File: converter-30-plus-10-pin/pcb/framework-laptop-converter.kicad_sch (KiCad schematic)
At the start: 6 parts, among them J1 20879-040E-01, J2 FFC2B28-40-G

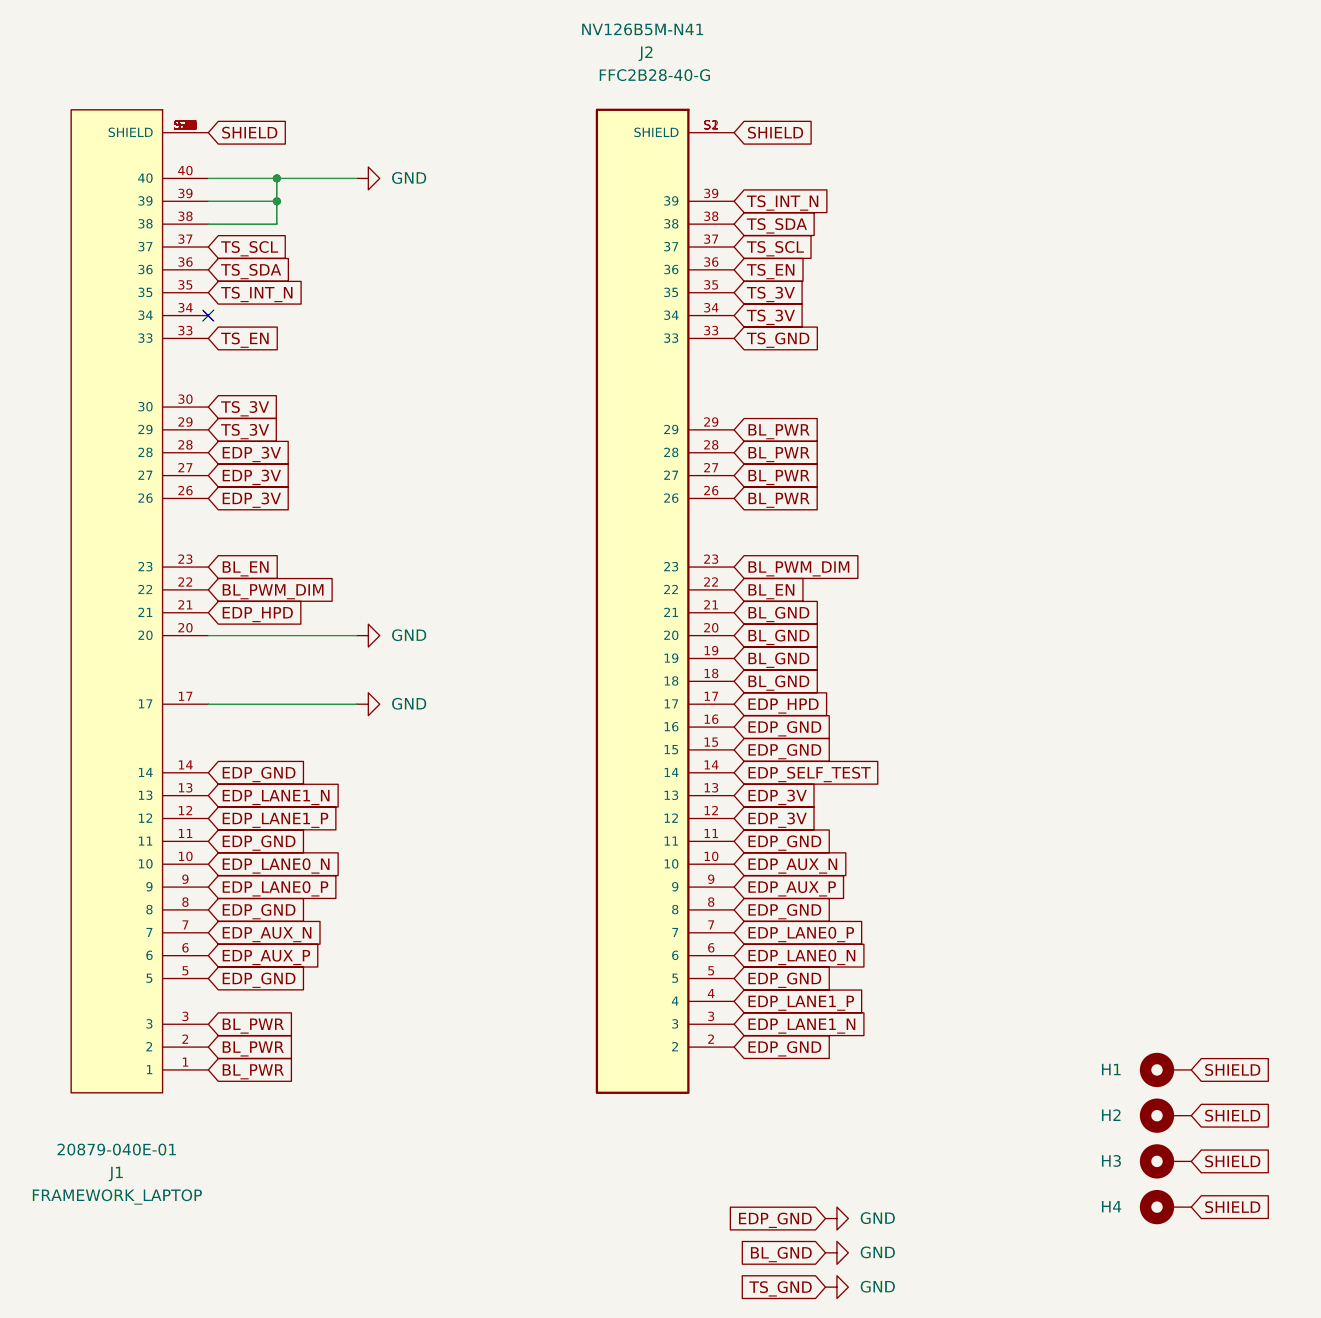
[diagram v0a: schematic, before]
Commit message: start migrating converter to framework's true pinout
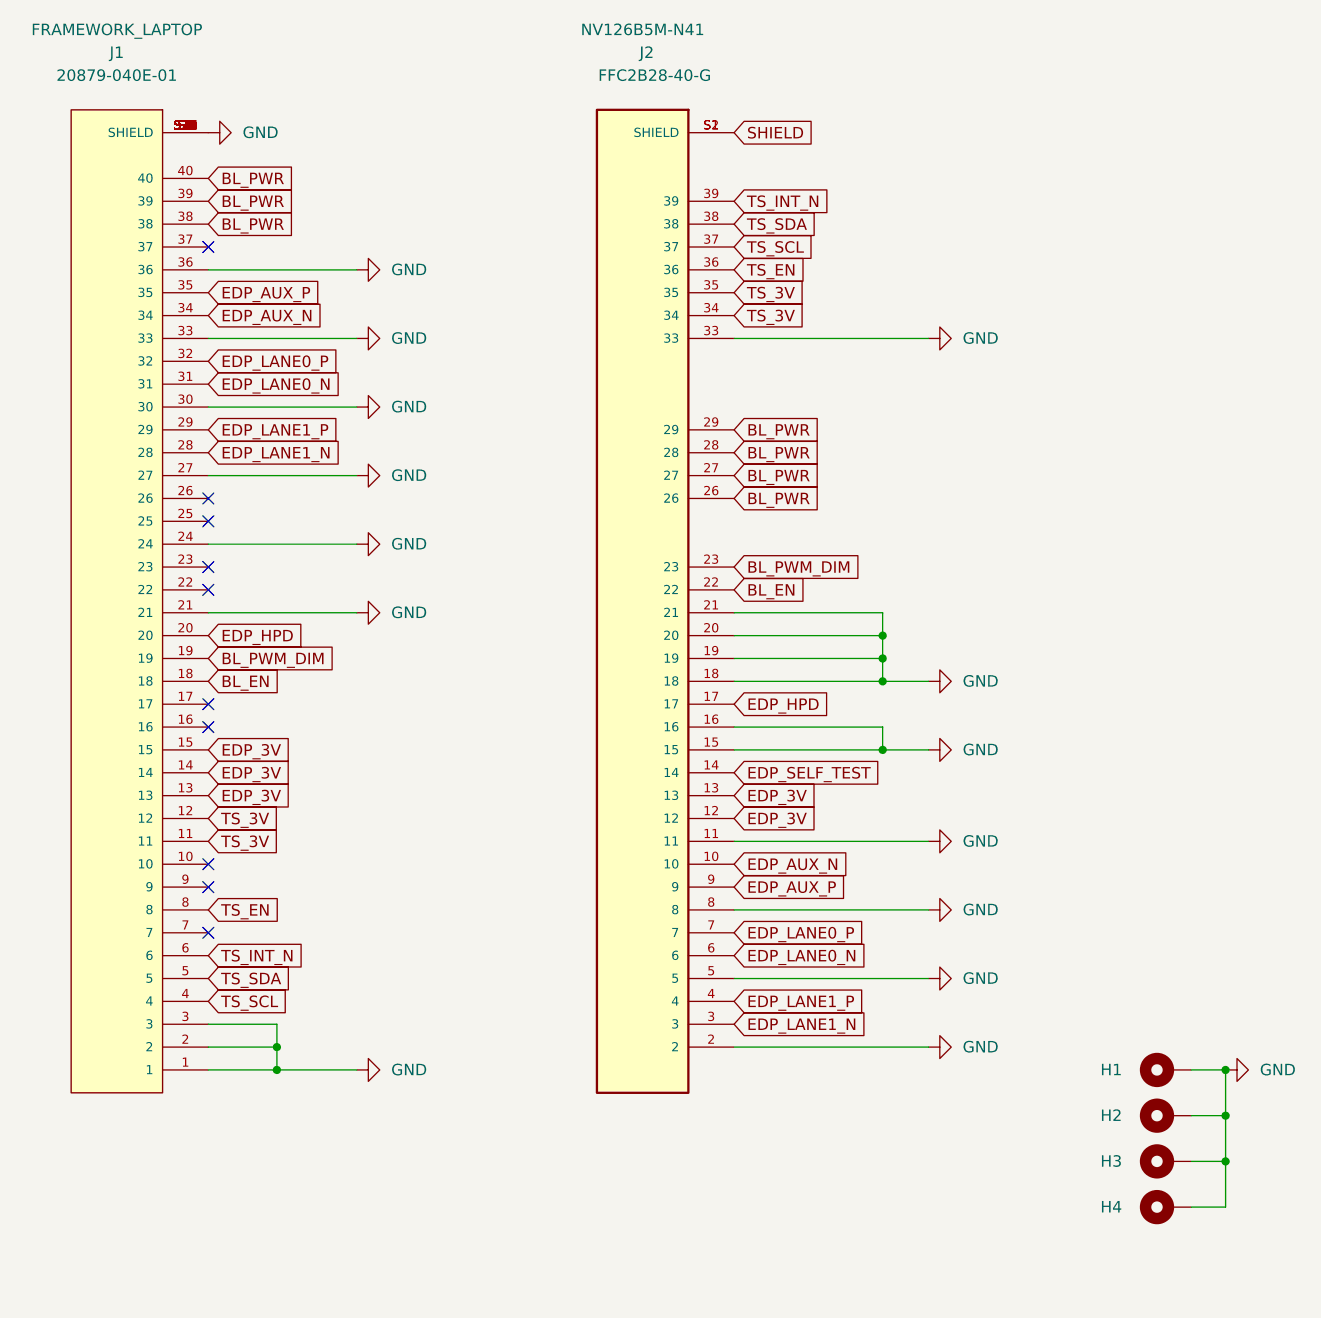
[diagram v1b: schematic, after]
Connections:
- net BL_EN: now also J1.18; no longer J1.23
- net BL_PWM_DIM: now also J1.19; no longer J1.22
- net BL_PWR: now also J1.38, J1.39, J1.40; no longer J1.1, J1.2, J1.3
- net EDP_3V: now also J1.13, J1.14, J1.15; no longer J1.26, J1.27, J1.28
- net EDP_AUX_N: now also J1.34; no longer J1.7
- net EDP_AUX_P: now also J1.35; no longer J1.6
- net EDP_HPD: now also J1.20; no longer J1.21
- net EDP_LANE0_N: now also J1.31; no longer J1.10
- net EDP_LANE0_P: now also J1.32; no longer J1.9
- net EDP_LANE1_N: now also J1.28; no longer J1.13
- net EDP_LANE1_P: now also J1.29; no longer J1.12
- net GND: now also H1.1, H2.1, H3.1, H4.1, J1.1, J1.2, J1.21, J1.24, J1.27, J1.3, J1.30, J1.33, J1.36, J1.S1 (SHIELD), J1.S10 (SHIELD), J1.S11 (SHIELD), J1.S12 (SHIELD), J1.S13 (SHIELD), J1.S14 (SHIELD), J1.S15 (SHIELD), J1.S16 (SHIELD), J1.S17 (SHIELD), J1.S18 (SHIELD), J1.S19 (SHIELD), J1.S2 (SHIELD), J1.S20 (SHIELD), J1.S21 (SHIELD), J1.S22 (SHIELD), J1.S23 (SHIELD), J1.S24 (SHIELD), J1.S25 (SHIELD), J1.S26 (SHIELD), J1.S27 (SHIELD), J1.S28 (SHIELD), J1.S29 (SHIELD), J1.S3 (SHIELD), J1.S30 (SHIELD), J1.S31 (SHIELD), J1.S32 (SHIELD), J1.S33 (SHIELD), J1.S34 (SHIELD), J1.S4 (SHIELD), J1.S5 (SHIELD), J1.S6 (SHIELD), J1.S7 (SHIELD), J1.S8 (SHIELD), J1.S9 (SHIELD); no longer J1.11, J1.14, J1.17, J1.20, J1.38, J1.39, J1.40, J1.5, J1.8
- net SHIELD: no longer H1.1, H2.1, H3.1, H4.1, J1.S1 (SHIELD), J1.S10 (SHIELD), J1.S11 (SHIELD), J1.S12 (SHIELD), J1.S13 (SHIELD), J1.S14 (SHIELD), J1.S15 (SHIELD), J1.S16 (SHIELD), J1.S17 (SHIELD), J1.S18 (SHIELD), J1.S19 (SHIELD), J1.S2 (SHIELD), J1.S20 (SHIELD), J1.S21 (SHIELD), J1.S22 (SHIELD), J1.S23 (SHIELD), J1.S24 (SHIELD), J1.S25 (SHIELD), J1.S26 (SHIELD), J1.S27 (SHIELD), J1.S28 (SHIELD), J1.S29 (SHIELD), J1.S3 (SHIELD), J1.S30 (SHIELD), J1.S31 (SHIELD), J1.S32 (SHIELD), J1.S33 (SHIELD), J1.S34 (SHIELD), J1.S4 (SHIELD), J1.S5 (SHIELD), J1.S6 (SHIELD), J1.S7 (SHIELD), J1.S8 (SHIELD), J1.S9 (SHIELD)
- net TS_3V: now also J1.11, J1.12; no longer J1.29, J1.30
- net TS_EN: now also J1.8; no longer J1.33
- net TS_INT_N: now also J1.6; no longer J1.35
- net TS_SCL: now also J1.4; no longer J1.37
- net TS_SDA: now also J1.5; no longer J1.36
- no-connect marks 1 -> 10

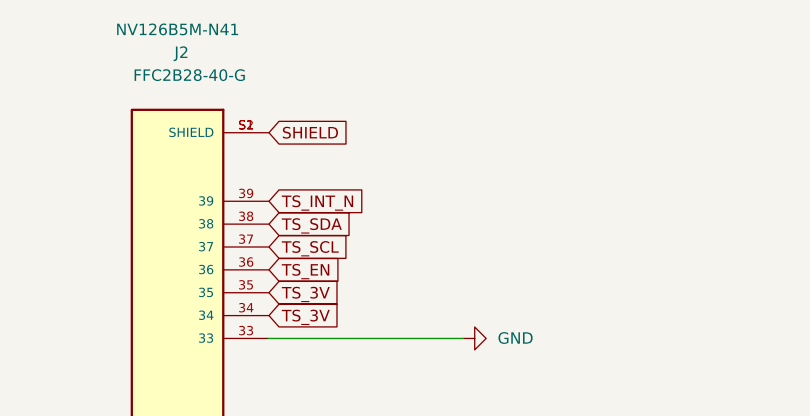
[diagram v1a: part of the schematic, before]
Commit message: converter: route edp lane 0 and aux + fix shield to ground
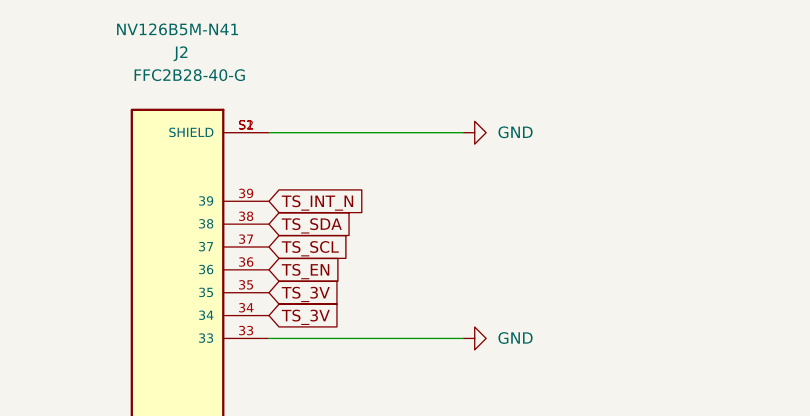
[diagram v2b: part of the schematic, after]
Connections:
- net SHIELD is gone; now on net GND: J2.S1 (SHIELD), J2.S2 (SHIELD)
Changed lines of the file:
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@@
+    (stroke (width 0) (type default) (color 0 0 0 0))
+  )
+  (wire (pts (xy 106.68 34.29) (xy 128.27 34.29))
     (stroke (width 0) (type default) (color 0 0 0 0))
   )
@@
     (effects (font (size 1.27 1.27)) (justify left))
     (property "Intersheet References" "${INTERSHEET_REFS}" (id 0) (at 57.6279 105.4894 0)
-      (effects (font (size 1.27 1.27)) (justify left) hide)
-    )
-  )
-  (global_label "SHIELD" (shape input) (at 106.68 34.29 0) (fields_autoplaced)
-    (effects (font (size 1.27 1.27)) (justify left))
-    (property "Intersheet References" "${INTERSHEET_REFS}" (id 0) (at 115.685 34.2106 0)
       (effects (font (size 1.27 1.27)) (justify left) hide)
     )
@@
     (pin "1")
   )
+  (symbol (lib_id "power:GND") (at 128.27 34.29 90) (unit 1)
+    (in_bom yes) (on_board yes) (fields_autoplaced)
+    (property "Reference" "#PWR?" (id 0) (at 134.62 34.29 0)
+      (effects (font (size 1.27 1.27)) hide)
+    )
+    (property "Value" "GND" (id 1) (at 132.08 34.2899 90)
+      (effects (font (size 1.27 1.27)) (justify right))
+    )
+    (property "Footprint" "" (id 2) (at 128.27 34.29 0)
+      (effects (font (size 1.27 1.27)) hide)
+    )
+    (property "Datasheet" "" (id 3) (at 128.27 34.29 0)
+      (effects (font (size 1.27 1.27)) hide)
+    )
+    (pin "1")
+  )
   (symbol (lib_id "Mechanical:MountingHole_Pad") (at 154.94 153.67 90) (unit 1)
     (in_bom yes) (on_board yes)
@@
       (reference "#PWR?") (unit 1) (value "GND") (footprint "")
     )
+    (path "/c65484eb-d2ac-483c-9646-1659e2d72b96"
+      (reference "#PWR?") (unit 1) (value "GND") (footprint "")
+    )

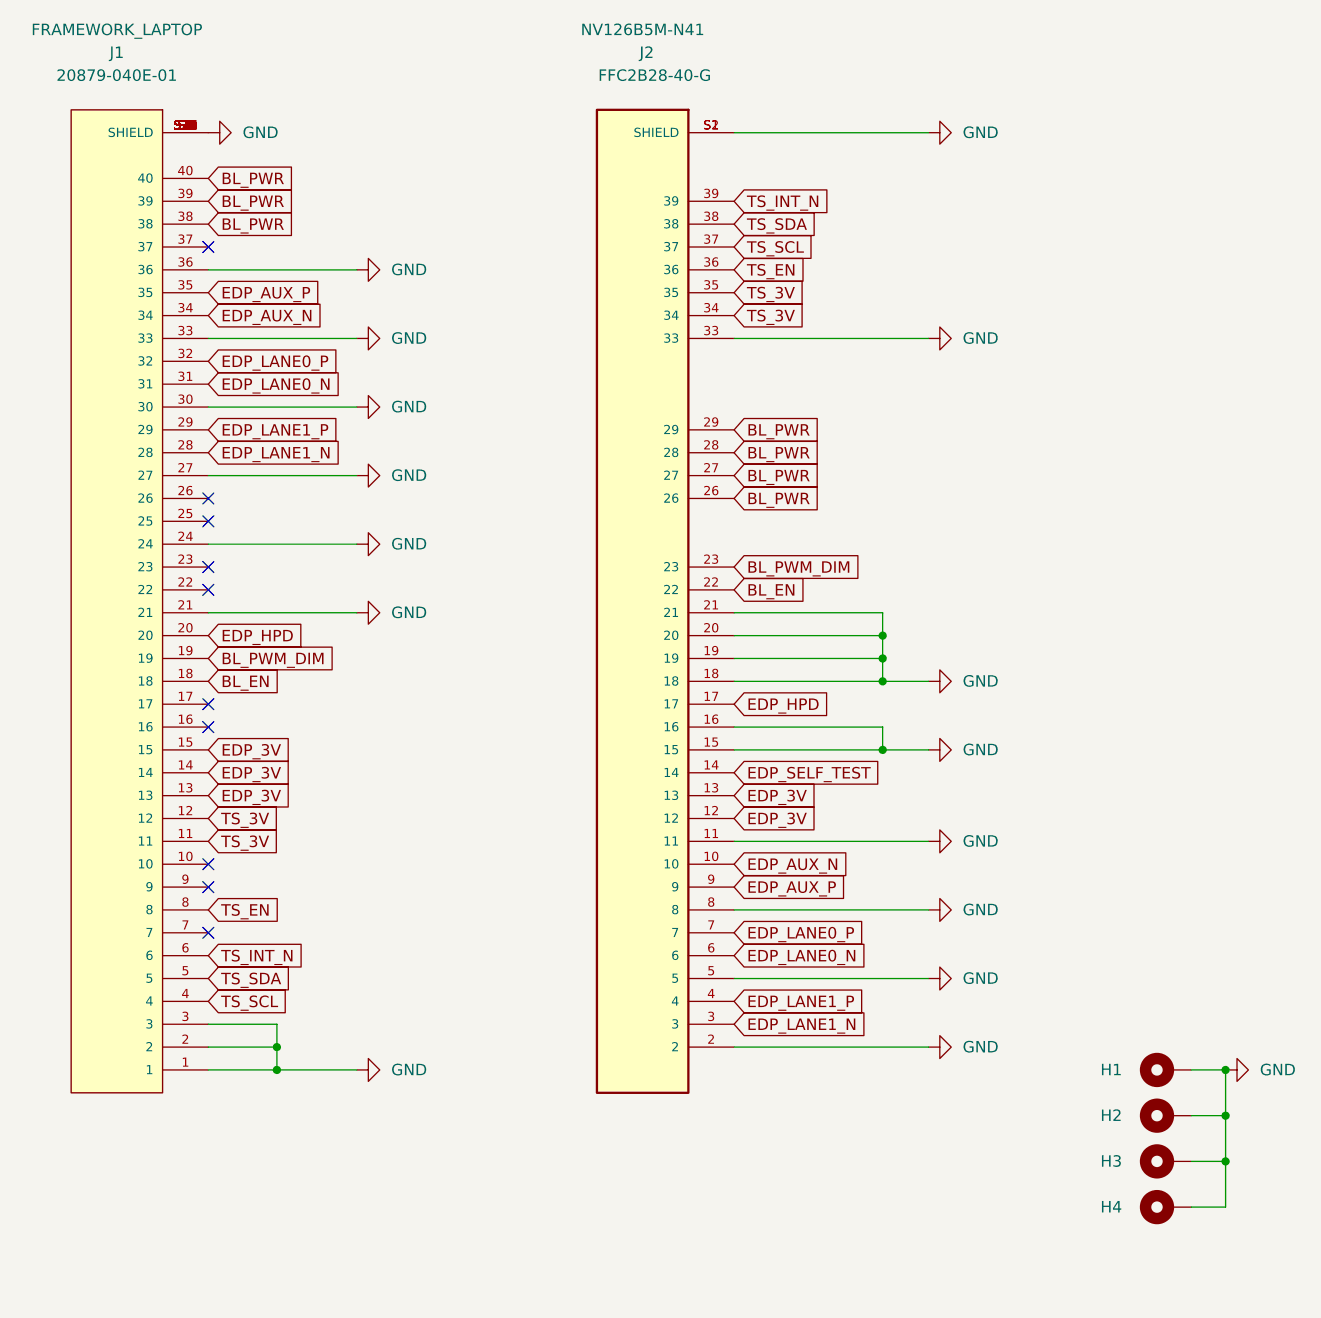
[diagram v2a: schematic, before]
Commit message: redo converter to use the 20455-040E
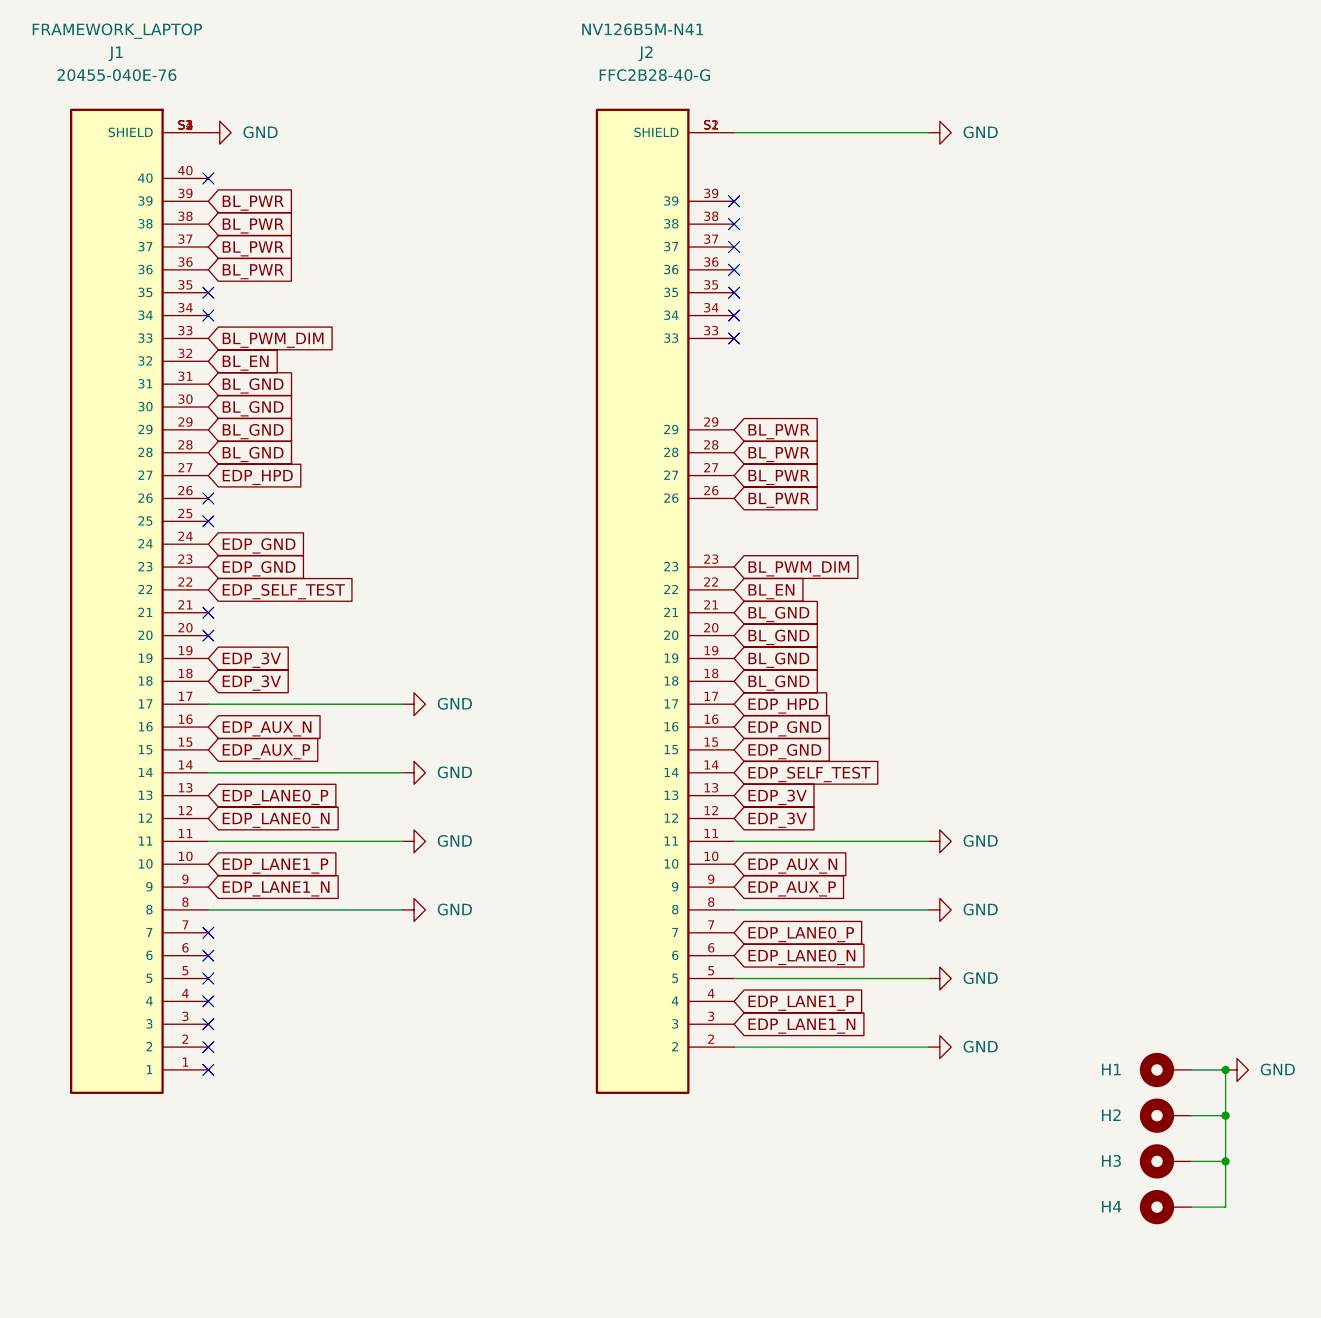
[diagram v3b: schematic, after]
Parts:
- J1: value 20879-040E-01 -> 20455-040E-76; footprint IPEX_20879-040E-01 -> IPEX_20455-040E-76; symbol 20879-040E-01:20879-040E-01 -> 20455-040E-76:20455-040E-76; STANDARD Manufacturer recommendations -> Manufacturer Recommendations
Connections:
- net BL_EN: now also J1.32; no longer J1.18
- net BL_PWM_DIM: now also J1.33; no longer J1.19
- net BL_PWR: now also J1.36, J1.37; no longer J1.40
- net EDP_3V: now also J1.18, J1.19; no longer J1.13, J1.14, J1.15
- net EDP_AUX_N: now also J1.16; no longer J1.34
- net EDP_AUX_P: now also J1.15; no longer J1.35
- net EDP_HPD: now also J1.27; no longer J1.20
- net EDP_LANE0_N: now also J1.12; no longer J1.31
- net EDP_LANE0_P: now also J1.13; no longer J1.32
- net EDP_LANE1_N: now also J1.9; no longer J1.28
- net EDP_LANE1_P: now also J1.10; no longer J1.29
- net EDP_SELF_TEST: now also J1.22
- net GND: now also J1.11, J1.14, J1.17, J1.8; no longer J1.1, J1.2, J1.21, J1.24, J1.27, J1.3, J1.30, J1.33, J1.36, J1.S10 (SHIELD), J1.S11 (SHIELD), J1.S12 (SHIELD), J1.S13 (SHIELD), J1.S14 (SHIELD), J1.S15 (SHIELD), J1.S16 (SHIELD), J1.S17 (SHIELD), J1.S18 (SHIELD), J1.S19 (SHIELD), J1.S20 (SHIELD), J1.S21 (SHIELD), J1.S22 (SHIELD), J1.S23 (SHIELD), J1.S24 (SHIELD), J1.S25 (SHIELD), J1.S26 (SHIELD), J1.S27 (SHIELD), J1.S28 (SHIELD), J1.S29 (SHIELD), J1.S30 (SHIELD), J1.S31 (SHIELD), J1.S32 (SHIELD), J1.S33 (SHIELD), J1.S34 (SHIELD), J1.S5 (SHIELD), J1.S6 (SHIELD), J1.S7 (SHIELD), J1.S8 (SHIELD), J1.S9 (SHIELD), J2.15, J2.16, J2.18, J2.19, J2.20, J2.21, J2.33
- net EDP_GND: now reaches J1.23
- net EDP_GND: now also J1.24, J2.15, J2.16
- removed net TS_3V: J1.11, J1.12, J2.34, J2.35
- net TS_EN: no longer names the net of J2.36
- net TS_EN: no longer J1.8
- net TS_INT_N: no longer names the net of J2.39
- net TS_INT_N: no longer J1.6
- net TS_SCL: no longer names the net of J2.37
- net TS_SCL: no longer J1.4
- net TS_SDA: no longer names the net of J2.38
- net TS_SDA: no longer J1.5
- new net BL_GND: J1.28, J1.29, J1.30, J1.31, J2.18, J2.19, J2.20, J2.21
- no-connect marks 10 -> 21

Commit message: clean up footprints & connections
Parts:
- J1: footprint IPEX_20455-040E-76 -> footprints:IPEX_20455-040E-76
- J2: footprint GCT_FFC2B28-40-G -> footprints:GCT_FFC2B28-40-G
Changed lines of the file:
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@@
       (effects (font (size 1.27 1.27)) (justify left))
     )
-    (property "Footprint" "GCT_FFC2B28-40-G" (id 2) (at 96.52 87.63 0)
+    (property "Footprint" "footprints:GCT_FFC2B28-40-G" (id 2) (at 96.52 87.63 0)
       (effects (font (size 1.27 1.27)) (justify left bottom) hide)
     )
@@
     (property "Reference" "J1" (id 0) (at 38.1 25.4 0))
     (property "Value" "20455-040E-76" (id 1) (at 38.1 27.94 0))
-    (property "Footprint" "IPEX_20455-040E-76" (id 2) (at 38.1 87.63 0)
+    (property "Footprint" "footprints:IPEX_20455-040E-76" (id 2) (at 38.1 87.63 0)
       (effects (font (size 1.27 1.27)) (justify left bottom) hide)
     )
@@
     )
     (path "/45b0ea5e-db31-4626-9deb-ab5e9ede7987"
-      (reference "J1") (unit 1) (value "20455-040E-76") (footprint "IPEX_20455-040E-76")
+      (reference "J1") (unit 1) (value "20455-040E-76") (footprint "footprints:IPEX_20455-040E-76")
     )
     (path "/23ca3b84-fefb-4da0-a3fe-ff0302049529"
-      (reference "J2") (unit 1) (value "FFC2B28-40-G") (footprint "GCT_FFC2B28-40-G")
-    )
-  )
+      (reference "J2") (unit 1) (value "FFC2B28-40-G") (footprint "footprints:GCT_FFC2B28-40-G")
+    )
+  )
